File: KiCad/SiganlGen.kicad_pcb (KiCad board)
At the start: 2 copper layers, 73 parts, among them J1 Barrel_Jack_MountingPin, J2 Conn_Coaxial, J3 LCD_Conn, J4 Enc_Conn, J5 Btn_Matrix, J6 Btn&Led, J7 PWR, Q1 BD135, Q2 BD136, U1 RaspberryPi_Pico, U2 MC34063AP, U3 LM7805_TO220, U4 LM337_TO220, U5 LM7810_TO220, U6 LM318H

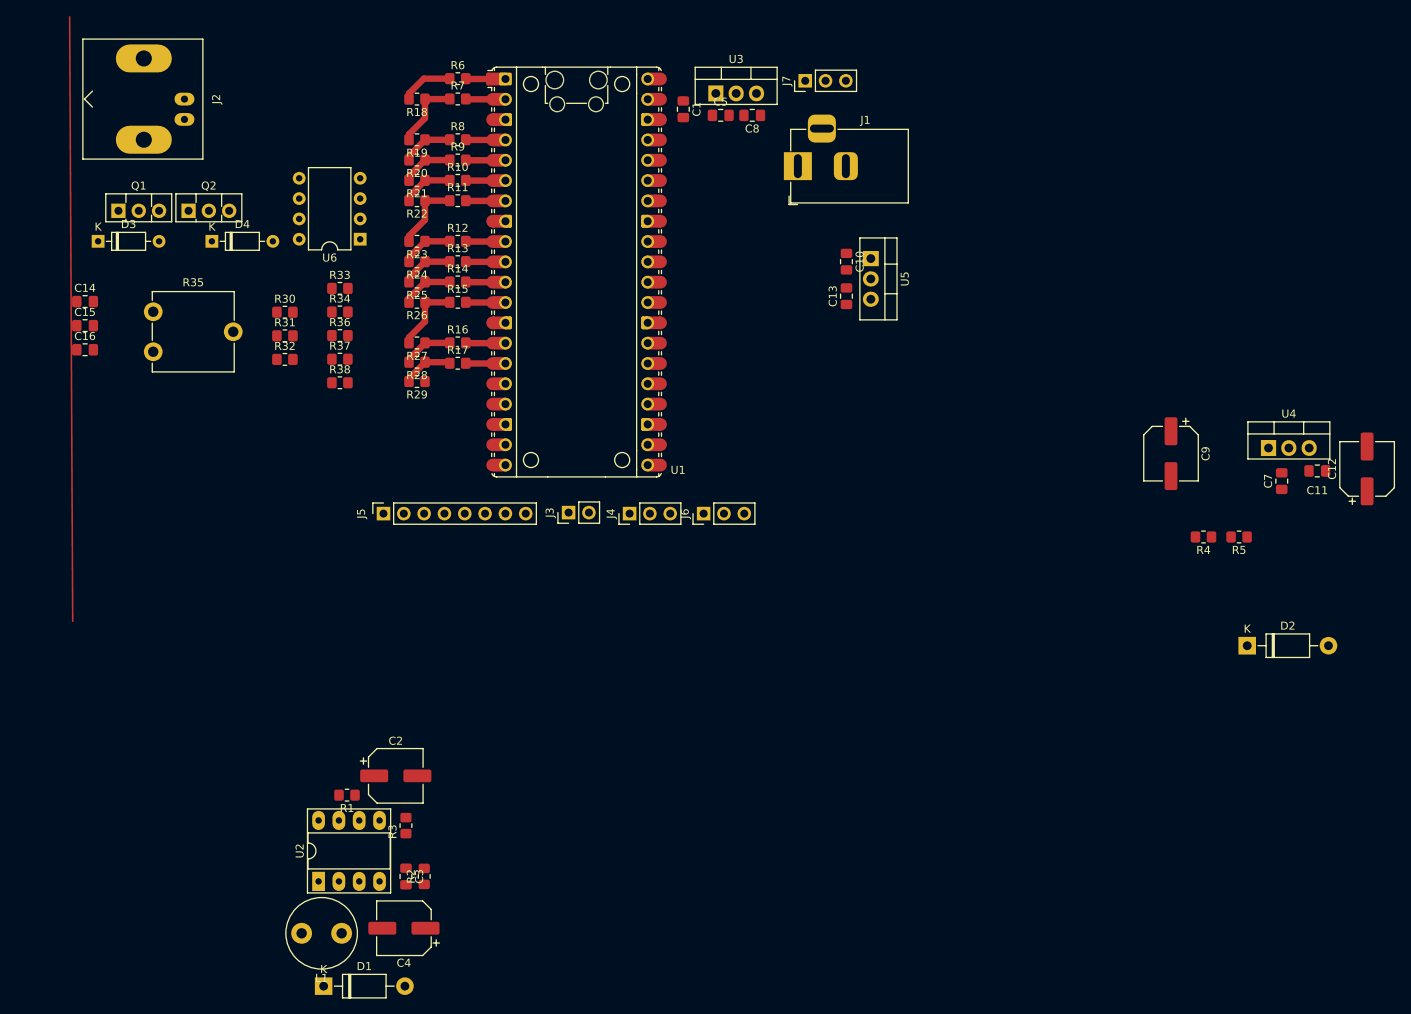
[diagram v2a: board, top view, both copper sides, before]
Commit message: Changed footprints, arrangement of elements on pcb
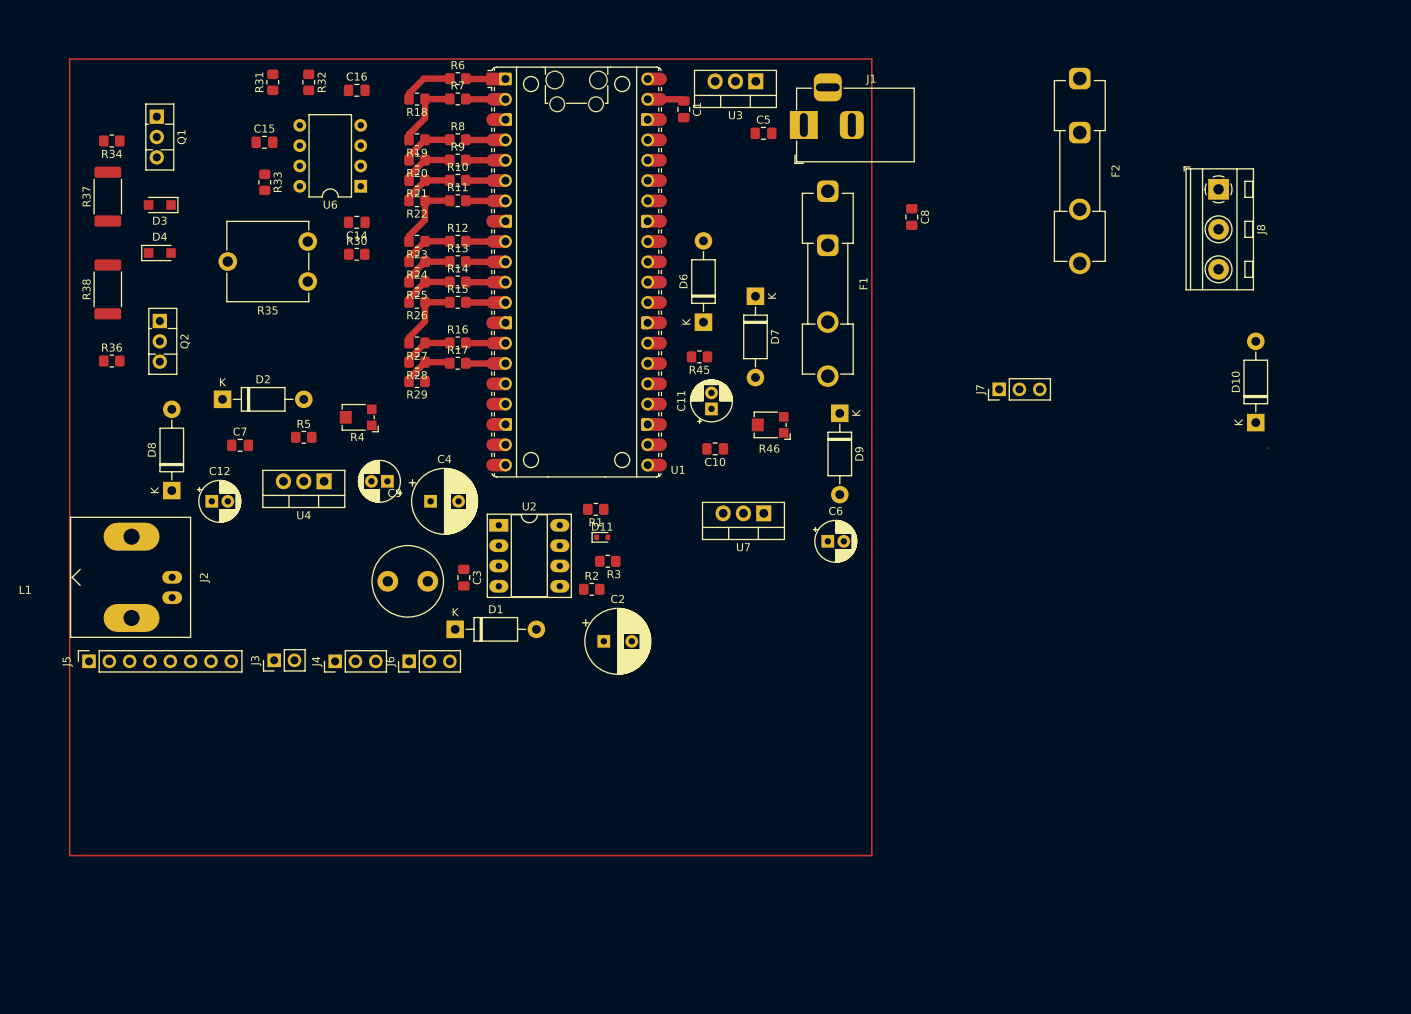
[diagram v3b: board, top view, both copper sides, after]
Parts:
- removed C13: 100n, Capacitor_SMD:C_0805_2012Metric_Pad1.18x1.45mm_HandSolder
- removed U5: LM7810_TO220, Package_TO_SOT_THT:TO-220-3_Vertical
- added C6: 22u, Capacitor_THT:CP_Radial_D5.0mm_P2.00mm, F.Cu at (189.0, 101.0)
- added D10: 1N4148WT, Diode_THT:D_DO-41_SOD81_P10.16mm_Horizontal, F.Cu at (242.5, 86.2)
- added D11: ESD5Zxx, Diode_SMD:D_SOD-523, F.Cu at (160.8, 100.5)
- added D6: 1N4007, Diode_THT:D_DO-41_SOD81_P10.16mm_Horizontal, F.Cu at (173.5, 73.6)
- added D7: 1N4007, Diode_THT:D_DO-41_SOD81_P10.16mm_Horizontal, F.Cu at (180.0, 70.4)
- added D8: 1N4007, Diode_THT:D_DO-41_SOD81_P10.16mm_Horizontal, F.Cu at (107.0, 94.7)
- added D9: 1N4148WT, Diode_THT:D_DO-41_SOD81_P10.16mm_Horizontal, F.Cu at (190.5, 85.0)
- added F1: Fuse, Fuse:Fuseholder_Clip-5x20mm_Keystone_3517_Inline_P23.11x6.76mm_D1.70mm_Horizontal, F.Cu at (189.0, 57.2)
- added F2: Fuse, Fuse:Fuseholder_Clip-5x20mm_Keystone_3517_Inline_P23.11x6.76mm_D1.70mm_Horizontal, F.Cu at (220.5, 43.1)
- added J8: Screw_Terminal_01x03, TerminalBlock_MetzConnect:TerminalBlock_MetzConnect_Type094_RT03503HBLU_1x03_P5.00mm_Horizontal, F.Cu at (237.8, 57.0)
- added R45: 100, Resistor_SMD:R_0805_2012Metric_Pad1.20x1.40mm_HandSolder, F.Cu at (173.0, 77.9)
- added R46: 1k, Potentiometer_SMD:Potentiometer_Bourns_TC33X_Vertical, F.Cu at (181.7, 86.4)
- added U7: LM317_TO-220, Package_TO_SOT_THT:TO-220-3_Vertical, F.Cu at (181.0, 97.5)
- C10: value 330n -> 100n
- C11: value 100n -> 22u; footprint Capacitor_SMD:C_0805_2012Metric_Pad1.18x1.45mm_HandSolder -> Capacitor_THT:CP_Radial_D5.0mm_P2.00mm
- C12, C9: footprint Capacitor_SMD:CP_Elec_6.3x5.3 -> Capacitor_THT:CP_Radial_D5.0mm_P2.00mm
- C2, C4: footprint Capacitor_SMD:CP_Elec_6.3x7.7 -> Capacitor_THT:CP_Radial_D8.0mm_P3.50mm
- D3, D4: footprint Diode_THT:D_DO-35_SOD27_P7.62mm_Horizontal -> Diode_SMD:Nexperia_CFP3_SOD-123W
- R37, R38: footprint Resistor_SMD:R_0805_2012Metric_Pad1.20x1.40mm_HandSolder -> Resistor_SMD:R_2512_6332Metric_Pad1.40x3.35mm_HandSolder
- R4: value 860 -> 1k; footprint Resistor_SMD:R_0805_2012Metric_Pad1.20x1.40mm_HandSolder -> Potentiometer_SMD:Potentiometer_Bourns_TC33X_Vertical
- moved C12 144.5 mm to (112.0, 96.0), turned to 0 degrees
- moved D2 131.7 mm to (113.3, 83.2)
- moved C7 130.3 mm to (115.5, 89.0), turned to 0 degrees
- moved U4 118.1 mm to (126.0, 93.5), turned to 180 degrees
- moved R5 117.6 mm to (123.5, 88.0), turned to 0 degrees
- moved R4 106.8 mm to (130.2, 85.5)
- moved C9 98.0 mm to (134.0, 93.5), turned to 180 degrees
- moved C11 76.1 mm to (174.5, 84.4), turned to 90 degrees
- moved J2 59.8 mm to (107.0, 105.5)
- moved C4 53.5 mm to (139.3, 96.0), turned to 0 degrees
- moved U2 49.9 mm to (147.9, 99.0), turned to 0 degrees
- moved D1 47.5 mm to (142.4, 112.0)
- moved R1 47.4 mm to (160.0, 97.0)
- moved C16 47.0 mm to (130.1, 44.6)
- moved J7 45.6 mm to (210.4, 82.0)
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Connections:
- C10 pad 1: +12V -> /Power Section/+12V
- C11 pad 1: GND -> +10V
- C11 pad 2: -10V -> GND
- C2 pad 1: +12V -> /Power Section/+12V
- C5 pad 1: +12V -> /Power Section/+12V
- C9 pad 2: Net-(U4-ADJ) -> Net-(D8-K)
- R1 pad 1: +12V -> /Power Section/+12V
- R4 pad 1: Net-(U4-ADJ) -> GND
- R4 pad 2: GND -> Net-(D8-K)
- R5 pad 2: Net-(U4-ADJ) -> Net-(D8-K)
- U2 pad 6: +12V -> /Power Section/+12V
- U3 pad 1: +12V -> /Power Section/+12V
- U4 pad 1: Net-(U4-ADJ) -> Net-(D8-K)
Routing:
- net +5V: track 0.00 -> 4.61 mm
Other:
- board text added: "+ stabilizer"
- board text added: "- stabilizer"

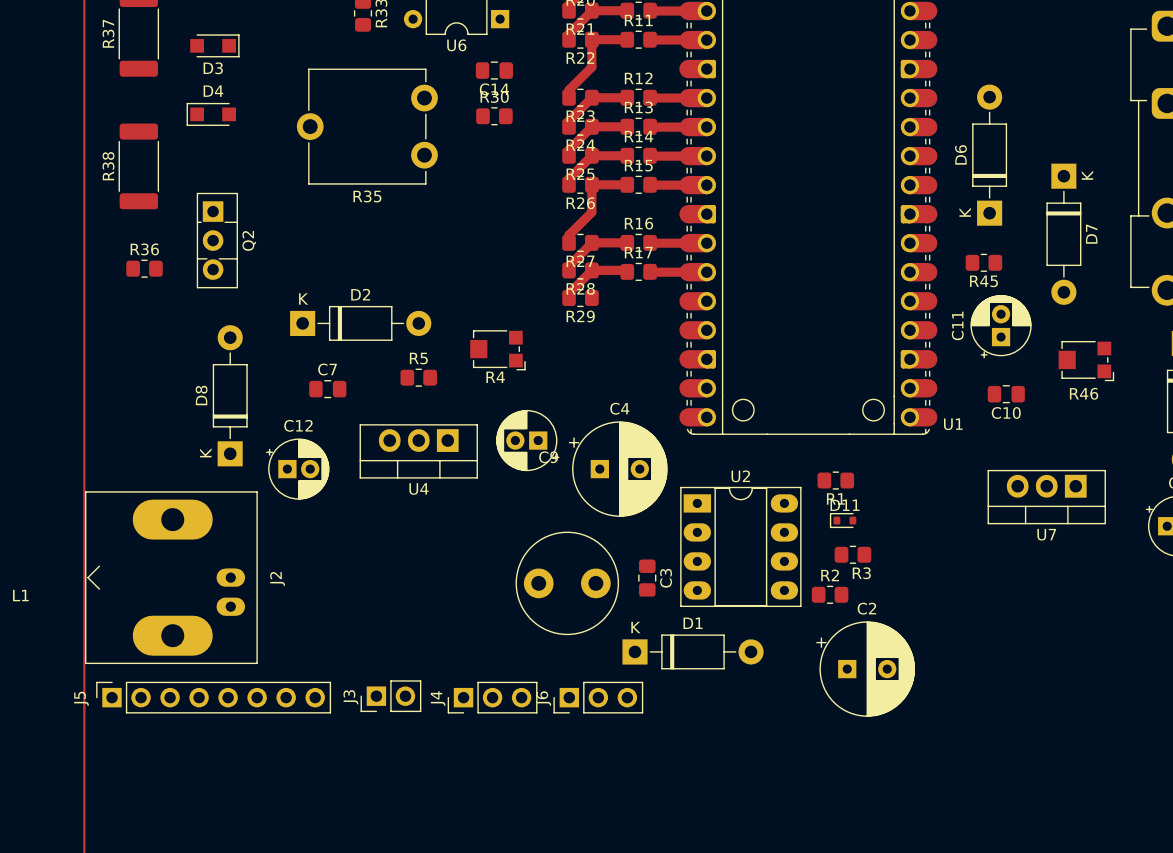
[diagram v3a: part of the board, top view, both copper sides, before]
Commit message: Tidied up schematic, changed footprints
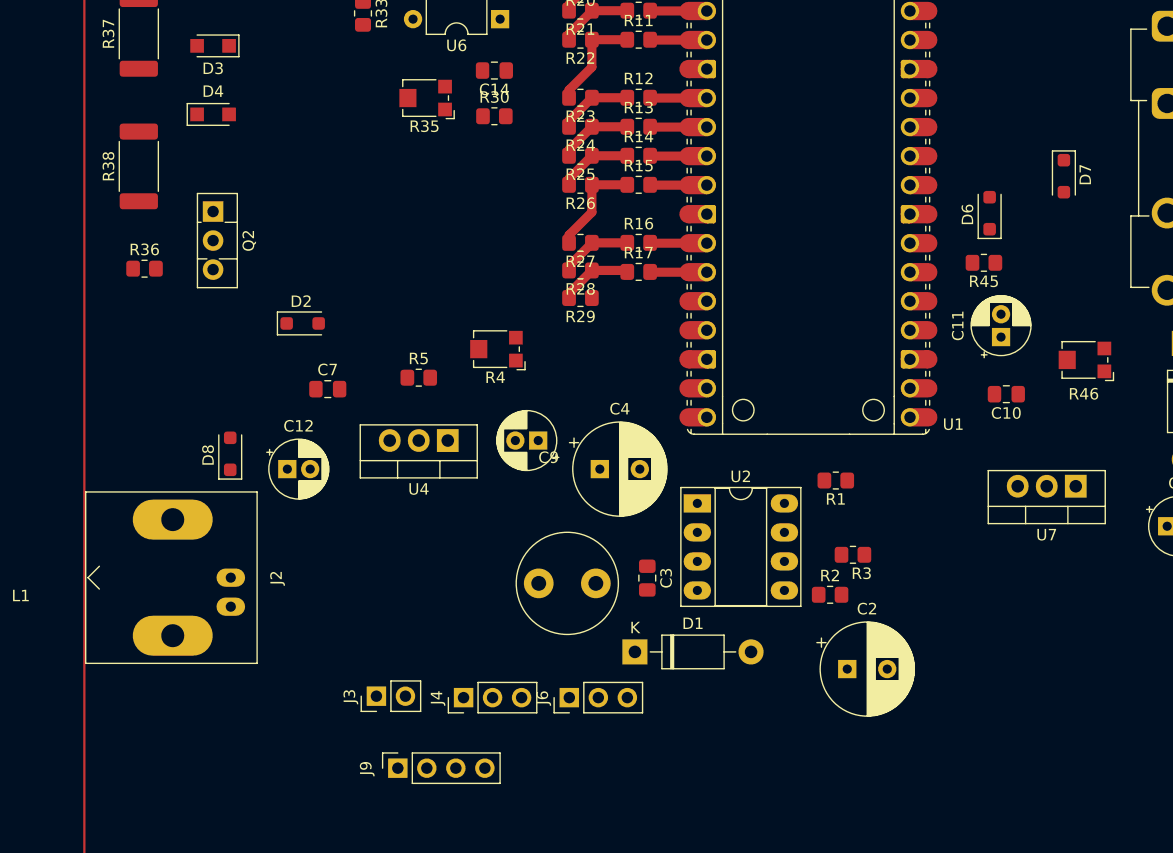
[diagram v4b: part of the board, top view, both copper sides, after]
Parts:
- removed D11: ESD5Zxx, Diode_SMD:D_SOD-523
- removed J5: Btn_Matrix, Connector_PinSocket_2.54mm:PinSocket_1x08_P2.54mm_Vertical
- added J9: Btn_Matrix, Connector_PinSocket_2.54mm:PinSocket_1x04_P2.54mm_Vertical, F.Cu at (121.7, 122.2)
- D2, D6, D7, D8: footprint Diode_THT:D_DO-41_SOD81_P10.16mm_Horizontal -> Diode_SMD:D_SOD-123F
- R35: footprint Potentiometer_THT:Potentiometer_ACP_CA9-V10_Vertical -> Potentiometer_SMD:Potentiometer_Bourns_TC33X_Vertical
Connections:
- net /ENC_CLK renamed /ENC.DT
- net /LCD_SCL renamed /LCD.SCL
- net /LCD_SDA renamed /LCD.SDA
- net /X0 renamed /DAC8
- net /X1 renamed /DAC9
- net /X2 renamed /DAC10
- net /X3 renamed /DAC11
- C10 pad 1: /Power Section/+12V -> +12V
- C2 pad 1: /Power Section/+12V -> +12V
- C5 pad 1: /Power Section/+12V -> +12V
- D6 pad 1: /Power Section/+12V -> +12V
- D9 pad 1: /Power Section/+12V -> +12V
- F1 pad 1: +12V -> Net-(F1-Pad1)
- F1 pad 2: /Power Section/+12V -> +12V
- J1 pad 1: +12V -> Net-(F1-Pad1)
- J1 pad 3: (no net) -> GND
- J4 pad 2: /ENC_DT -> /ENC.CLK
- J4 pad 3: /ENC_SW -> /ENC.SW
- J6 pad 1: /SW1_OUT -> /UI.OUT0
- J6 pad 2: /SW2_OUT -> /UI.OUT1
- J6 pad 3: /LED1_IN -> /UI.IN0
- R1 pad 1: /Power Section/+12V -> +12V
- U1 pad 16: /Y0 -> /MUX0
- U1 pad 17: /Y1 -> /MUX1
- U1 pad 19: /Y2 -> /MUX2
- U1 pad 20: /Y3 -> /MUX3
- U1 pad 24: /ENC_DT -> /ENC.SW
- U1 pad 26: /ENC_SW -> /ENC.CLK
- U1 pad 27: /LED1_IN -> unconnected-(U1-GPIO21-Pad27)
- U1 pad 29: /SW2_OUT -> unconnected-(U1-GPIO22-Pad29)
- U1 pad 31: /SW1_OUT -> /UI.IN0
- U1 pad 32: unconnected-(U1-GPIO27_ADC1-Pad32)_0 -> /UI.OUT1
- U1 pad 34: unconnected-(U1-GPIO28_ADC2-Pad34)_0 -> /UI.OUT0
- U2 pad 6: /Power Section/+12V -> +12V
- U3 pad 1: /Power Section/+12V -> +12V
- U7 pad 3: /Power Section/+12V -> +12V

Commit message: Alfa version of PCB design
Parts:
- added C13: 100u, Capacitor_THT:CP_Radial_D5.0mm_P2.50mm, F.Cu at (191.9, 61.8)
- added C17: 100u, Capacitor_THT:CP_Radial_D5.0mm_P2.50mm, F.Cu at (175.9, 88.9)
- added C18: 100n, Capacitor_SMD:C_0805_2012Metric_Pad1.18x1.45mm_HandSolder, B.Cu at (119.9, 68.2)
- added C19: 100n, Capacitor_SMD:C_0805_2012Metric_Pad1.18x1.45mm_HandSolder, B.Cu at (131.4, 68.2)
- C10, C15, C16, C3, C7, D2, D6, D7, D8, R2, R3, R31, R32, R45, R5: moved to B.Cu
- C11, C12: value 22u -> 100u; footprint Capacitor_THT:CP_Radial_D5.0mm_P2.00mm -> Capacitor_THT:CP_Radial_D5.0mm_P2.50mm
- C2, C4: value 220u -> 100u; footprint Capacitor_THT:CP_Radial_D8.0mm_P3.50mm -> Capacitor_THT:CP_Radial_D5.0mm_P2.50mm
- C6, C9: value 22u -> 10u; footprint Capacitor_THT:CP_Radial_D5.0mm_P2.00mm -> Capacitor_SMD:C_0805_2012Metric_Pad1.18x1.45mm_HandSolder; moved to B.Cu
- moved J8 135.2 mm to (335.7, 150.3)
- moved D10 135.2 mm to (340.3, 179.4)
- moved F2 135.2 mm to (318.3, 136.4)
- moved D8 94.0 mm to (196.4, 65.7)
- moved D2 87.3 mm to (197.7, 60.6), turned to -90 degrees
- moved C7 87.2 mm to (200.0, 67.6)
- moved C2 82.5 mm to (120.1, 41.9)
- moved U4 80.2 mm to (201.1, 65.0), turned to 90 degrees
- moved R5 73.4 mm to (193.2, 65.0), turned to -90 degrees
- moved C12 68.8 mm to (173.4, 64.8), turned to -90 degrees
- moved R4 67.3 mm to (194.5, 65.7), turned to 0 degrees
- moved C9 63.6 mm to (192.6, 68.8), turned to 0 degrees
- moved L1 61.1 mm to (184.2, 64.8)
- moved D1 57.1 mm to (182.9, 71.8), turned to 180 degrees
- moved C4 55.8 mm to (125.8, 41.9)
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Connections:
- C12 pad 2: -10V -> -12V
- C2 pad 1: +12V -> +10V
- C4 pad 2: -12V -> -10V
- J4 pad 1: /ENC.DT -> /ENC.CLK
- J4 pad 2: /ENC.CLK -> /ENC.DT
- J7 pad 1: +5V -> +3V3
- J7 pad 2: +3V3 -> +5V
- J9 pad 3: /MUX2 -> /MUX3
- J9 pad 4: /MUX3 -> /MUX2
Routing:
- net +10V: track 0.00 -> 158.4 mm
- net +12V: track 0.00 -> 154.8 mm
- net -10V: track 0.00 -> 150.0 mm
- net -12V: track 0.04 -> 61.8 mm
- net /UI.OUT0: track 0.00 -> 44.8 mm
- net /UI.OUT1: track 0.00 -> 39.5 mm
- net /UI.IN0: track 0.00 -> 35.1 mm
- net Net-(F1-Pad1): track 0.00 -> 29.2 mm
- net /ENC.CLK: track 0.00 -> 22.0 mm
- net Net-(D3-K): track 0.00 -> 21.2 mm
- net /MUX0: track 0.00 -> 19.9 mm
- net Net-(J2-In): track 0.00 -> 19.6 mm
- net /ENC.DT: track 0.00 -> 18.6 mm
- net /MUX1: track 0.00 -> 17.9 mm
- net Net-(D7-A): track 0.00 -> 17.7 mm
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- added copper zone on B.Cu, net GND
- added copper zone on F.Cu, net GND
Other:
- board outline added: 94.6 x 64.8 mm
- board text removed: "+ stabilizer"
- board text removed: "- stabilizer"
- board text removed: "DC-DC inverter"

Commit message: PCB update
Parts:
- moved C10 13.5 mm to (197.5, 54.5)
- moved C6 13.2 mm to (199.5, 40.5)
- moved D2 9.94 mm to (197.0, 70.5)
- moved R46 9.39 mm to (193.7, 41.5)
- moved C7 8.62 mm to (201.0, 59.0)
- moved D7 5.27 mm to (197.5, 44.9), turned to 90 degrees
- moved D6 5.02 mm to (197.5, 50.1), turned to 90 degrees
- moved R4 4.66 mm to (194.6, 61.0)
- moved R5 4.66 mm to (193.3, 60.4)
- moved U7 4.61 mm to (201.0, 44.9), turned to -90 degrees
- moved C11 3.95 mm to (192.0, 50.5), turned to -90 degrees
- moved C13 2.94 mm to (189.0, 61.7)
- moved C9 2.86 mm to (193.0, 66.0)
- moved R45 2.03 mm to (195.0, 47.5), turned to -90 degrees
- moved D8 1.86 mm to (197.0, 63.9), turned to -90 degrees
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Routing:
- net +12V: track 154.8 -> 147.1 mm
- net Net-(D7-A): track 17.7 -> 22.8 mm
- net +10V: track 158.4 -> 154.6 mm
- net -12V: track 61.8 -> 65.1 mm
- net Net-(D8-K): track 17.5 -> 16.8 mm
- net -10V: track 150.0 -> 149.4 mm
- net Net-(Q1-E): track 7.85 -> 8.36 mm
- net GND: vias 116 -> 148
- removed copper zone on B.Cu, net GND
- removed copper zone on F.Cu, net GND

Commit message: PCB design
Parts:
- removed D10: 1N4148WT, Diode_THT:D_DO-41_SOD81_P10.16mm_Horizontal
- removed F2: Fuse, Fuse:Fuseholder_Clip-5x20mm_Keystone_3517_Inline_P23.11x6.76mm_D1.70mm_Horizontal
- removed J8: Screw_Terminal_01x03, TerminalBlock_MetzConnect:TerminalBlock_MetzConnect_Type094_RT03503HBLU_1x03_P5.00mm_Horizontal
- added R39: 100, Resistor_SMD:R_0805_2012Metric_Pad1.20x1.40mm_HandSolder, F.Cu at (127.9, 62.0)
- added R40: 100, Resistor_SMD:R_0805_2012Metric_Pad1.20x1.40mm_HandSolder, F.Cu at (127.9, 64.6)
- added REF**: MountingHole_3.2mm_M3_ISO14580_Pad, MountingHole:MountingHole_3.2mm_M3_ISO14580_Pad, F.Cu at (184.2, 87.0)
- added REF**: MountingHole_3.2mm_M3_ISO14580_Pad, MountingHole:MountingHole_3.2mm_M3_ISO14580_Pad, F.Cu at (203.2, 38.1)
- added REF**: MountingHole_3.2mm_M3_ISO14580_Pad, MountingHole:MountingHole_3.2mm_M3_ISO14580_Pad, F.Cu at (114.3, 38.1)
- added REF**: MountingHole_3.2mm_M3_ISO14580_Pad, MountingHole:MountingHole_3.2mm_M3_ISO14580_Pad, F.Cu at (134.0, 87.0)
- C10: moved to F.Cu
- D9: footprint Diode_THT:D_DO-41_SOD81_P10.16mm_Horizontal -> Diode_THT:D_DO-41_SOD81_P5.08mm_Vertical_KathodeUp
- R35: value 100 -> 1k
- moved C13 9.17 mm to (190.8, 52.7), turned to -90 degrees
- moved C9 8.83 mm to (194.3, 57.3), turned to -90 degrees
- moved D2 8.27 mm to (196.8, 62.2), turned to 90 degrees
- moved C7 7.25 mm to (199.9, 66.2)
- moved U4 5.58 mm to (201.0, 58.4)
- moved C6 4.90 mm to (194.6, 40.5)
- moved C10 4.86 mm to (202.3, 54.0)
- moved C3 4.84 mm to (178.4, 76.2)
- moved C19 4.56 mm to (127.0, 69.2), turned to 0 degrees
- moved R45 4.36 mm to (198.1, 44.5)
- moved R4 4.11 mm to (196.3, 57.3)
- moved C11 3.96 mm to (190.8, 46.7)
- moved R3 3.70 mm to (174.0, 77.5), turned to 0 degrees
- moved L1 3.46 mm to (182.9, 62.1)
- moved R46 3.42 mm to (196.2, 43.8)
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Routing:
- net +12V: track 147.1 -> 104.8 mm
- net Net-(F1-Pad1): track 29.2 -> 0.00 mm
- net -12V: track 65.1 -> 42.7 mm
- net Net-(U2-DC): track 0.00 -> 20.7 mm
- net Net-(D7-A): track 22.8 -> 2.88 mm
- net Net-(D8-K): track 16.8 -> 4.15 mm
- net +10V: track 154.6 -> 146.1 mm
- net Net-(R39-Pad1): track 0.00 -> 2.54 mm
- net Net-(D4-A): track 3.30 -> 5.69 mm
- net Net-(U2-TC): track 6.56 -> 4.76 mm
- net -10V: track 149.4 -> 147.6 mm
- net Net-(J2-In): track 19.6 -> 18.6 mm
- net /Output Stage/DAC_OUT: track 19.0 -> 19.6 mm
- net Net-(D4-K): track 6.08 -> 5.56 mm
- net GND: vias 148 -> 541
- added copper zone on B.Cu, net +10V
- added copper zone on F.Cu, net +12V
- added copper zone on B.Cu, net -12V
- added copper zone on B.Cu, net GND
- added copper zone on F.Cu, net GND
- added copper zone on B.Cu, net Net-(D7-A)
- added copper zone on B.Cu, net Net-(D8-K)
- added copper zone on F.Cu, net Net-(F1-Pad1)
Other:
- board size 94.6 x 64.8 mm -> 96.5 x 67.3 mm
